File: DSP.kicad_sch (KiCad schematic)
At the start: 26 parts, among them J2 Conn_01x04, J3 Conn_01x04, J4 MEM2067-02-180-00-A_REVB, U4 STM32F401RBTx, U5 23K256, Y1 16MHz

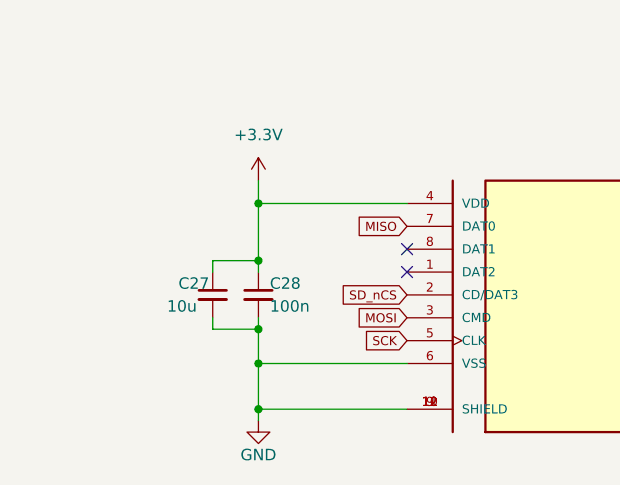
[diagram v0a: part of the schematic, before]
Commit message: added teardrops to increase yield&quality, also tuned usb data line skew
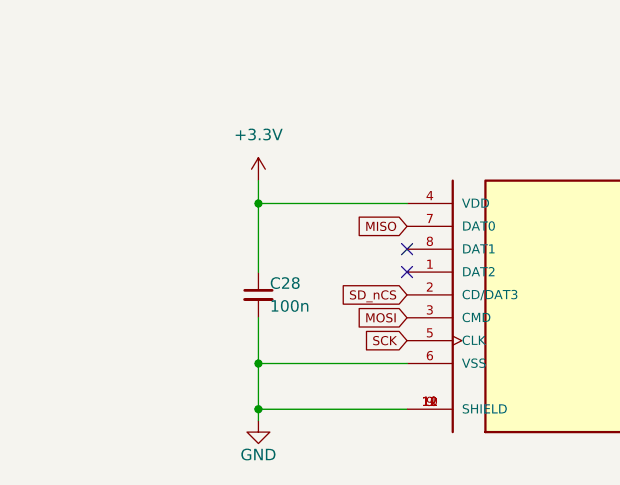
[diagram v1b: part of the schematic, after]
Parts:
- removed C27: 10u, Capacitor_SMD:C_0603_1608Metric_Pad1.08x0.95mm_HandSolder, symbol Device:C_Small
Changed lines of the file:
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@@
   (junction (at 60.96 36.83) (diameter 0) (color 0 0 0 0)
   )
-  (junction (at 53.34 161.29) (diameter 0) (color 0 0 0 0)
-  )
   (junction (at 30.48 40.64) (diameter 0) (color 0 0 0 0)
   )
@@
   )
   (junction (at 66.04 93.98) (diameter 0) (color 0 0 0 0)
-  )
-  (junction (at 53.34 168.91) (diameter 0) (color 0 0 0 0)
   )
   (junction (at 116.84 34.29) (diameter 0) (color 0 0 0 0)
@@
     (stroke (width 0) (type default))
   )
-  (wire (pts (xy 53.34 161.29) (xy 48.26 161.29))
-    (stroke (width 0) (type default))
-  )
   (wire (pts (xy 66.04 77.47) (xy 66.04 74.93))
     (stroke (width 0) (type default))
@@
     (stroke (width 0) (type default))
   )
-  (wire (pts (xy 53.34 168.91) (xy 53.34 172.72))
+  (wire (pts (xy 53.34 167.64) (xy 53.34 172.72))
     (stroke (width 0) (type default))
   )
@@
     (stroke (width 0) (type default))
   )
-  (wire (pts (xy 48.26 167.64) (xy 48.26 168.91))
-    (stroke (width 0) (type default))
-  )
   (wire (pts (xy 66.04 93.98) (xy 74.93 93.98))
     (stroke (width 0) (type default))
@@
     (stroke (width 0) (type default))
   )
-  (wire (pts (xy 48.26 161.29) (xy 48.26 162.56))
-    (stroke (width 0) (type default))
-  )
   (wire (pts (xy 92.71 53.34) (xy 92.71 52.07))
     (stroke (width 0) (type default))
@@
     (stroke (width 0) (type default))
   )
-  (wire (pts (xy 53.34 161.29) (xy 53.34 162.56))
-    (stroke (width 0) (type default))
-  )
   (wire (pts (xy 74.93 93.98) (xy 74.93 91.44))
     (stroke (width 0) (type default))
@@
     (stroke (width 0) (type default))
   )
-  (wire (pts (xy 53.34 168.91) (xy 48.26 168.91))
-    (stroke (width 0) (type default))
-  )
   (wire (pts (xy 214.63 97.79) (xy 214.63 99.06))
     (stroke (width 0) (type default))
@@
     (stroke (width 0) (type default))
   )
-  (wire (pts (xy 53.34 167.64) (xy 53.34 168.91))
-    (stroke (width 0) (type default))
-  )
   (wire (pts (xy 55.88 93.98) (xy 66.04 93.98))
     (stroke (width 0) (type default))
@@
     (stroke (width 0) (type default))
   )
-  (wire (pts (xy 53.34 154.94) (xy 53.34 161.29))
+  (wire (pts (xy 53.34 154.94) (xy 53.34 162.56))
     (stroke (width 0) (type default))
   )
@@
         )
       )
-    )
-  )
-  (symbol (lib_id "Device:C_Small") (at 48.26 165.1 0) (unit 1)
-    (in_bom yes) (on_board yes) (dnp no)
-    (property "Reference" "C27" (at 44.45 163.83 0)
-      (effects (font (size 1.27 1.27)) (justify left))
-    )
-    (property "Value" "10u" (at 43.18 166.37 0)
-      (effects (font (size 1.27 1.27)) (justify left))
-    )
-    (property "Footprint" "Capacitor_SMD:C_0603_1608Metric_Pad1.08x0.95mm_HandSolder" (at 48.26 165.1 0)
-      (effects (font (size 1.27 1.27)) hide)
-    )
-    (property "Datasheet" "~" (at 48.26 165.1 0)
-      (effects (font (size 1.27 1.27)) hide)
-    )
-    (pin "1")
-    (pin "2")
-    (instances
-      (project "Apollo - DSP"
-        (path "/e63e39d7-6ac0-4ffd-8aa3-1841a4541b55/65c41d2a-7921-40f6-8a66-43d43155f96a"
-          (reference "C27") (unit 1)
-        )
-      )

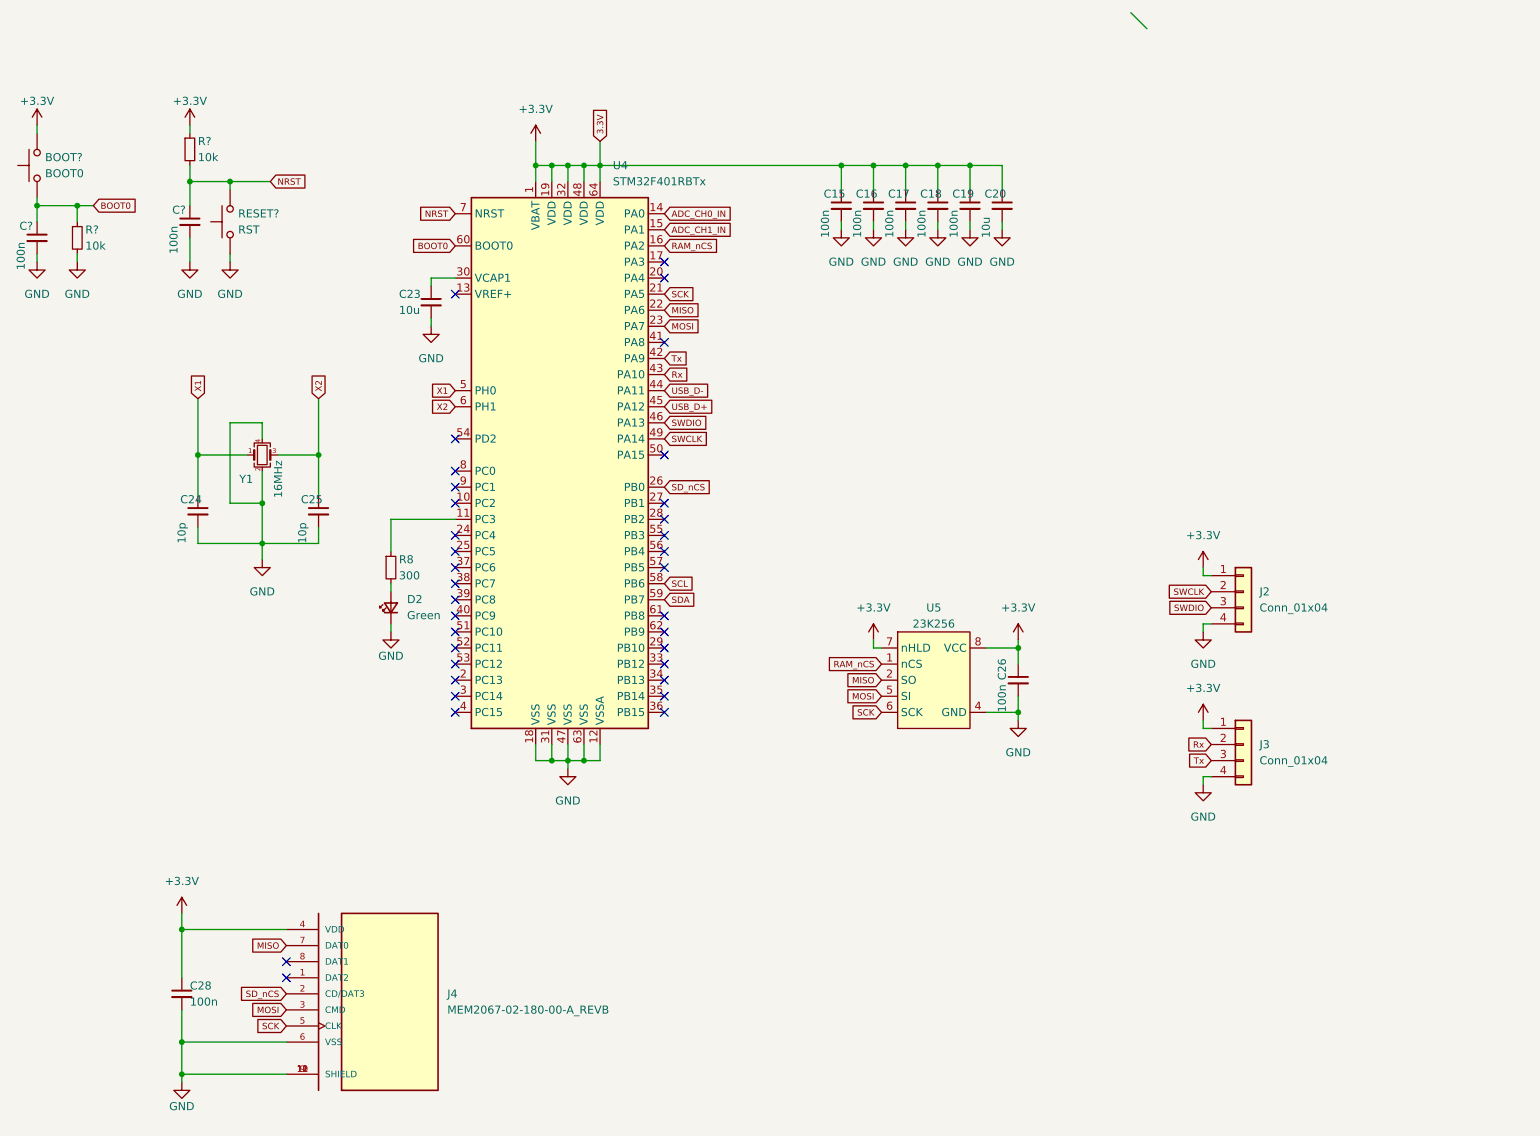
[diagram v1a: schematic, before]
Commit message: fixed bootloader setting to SWD, removed boot button.
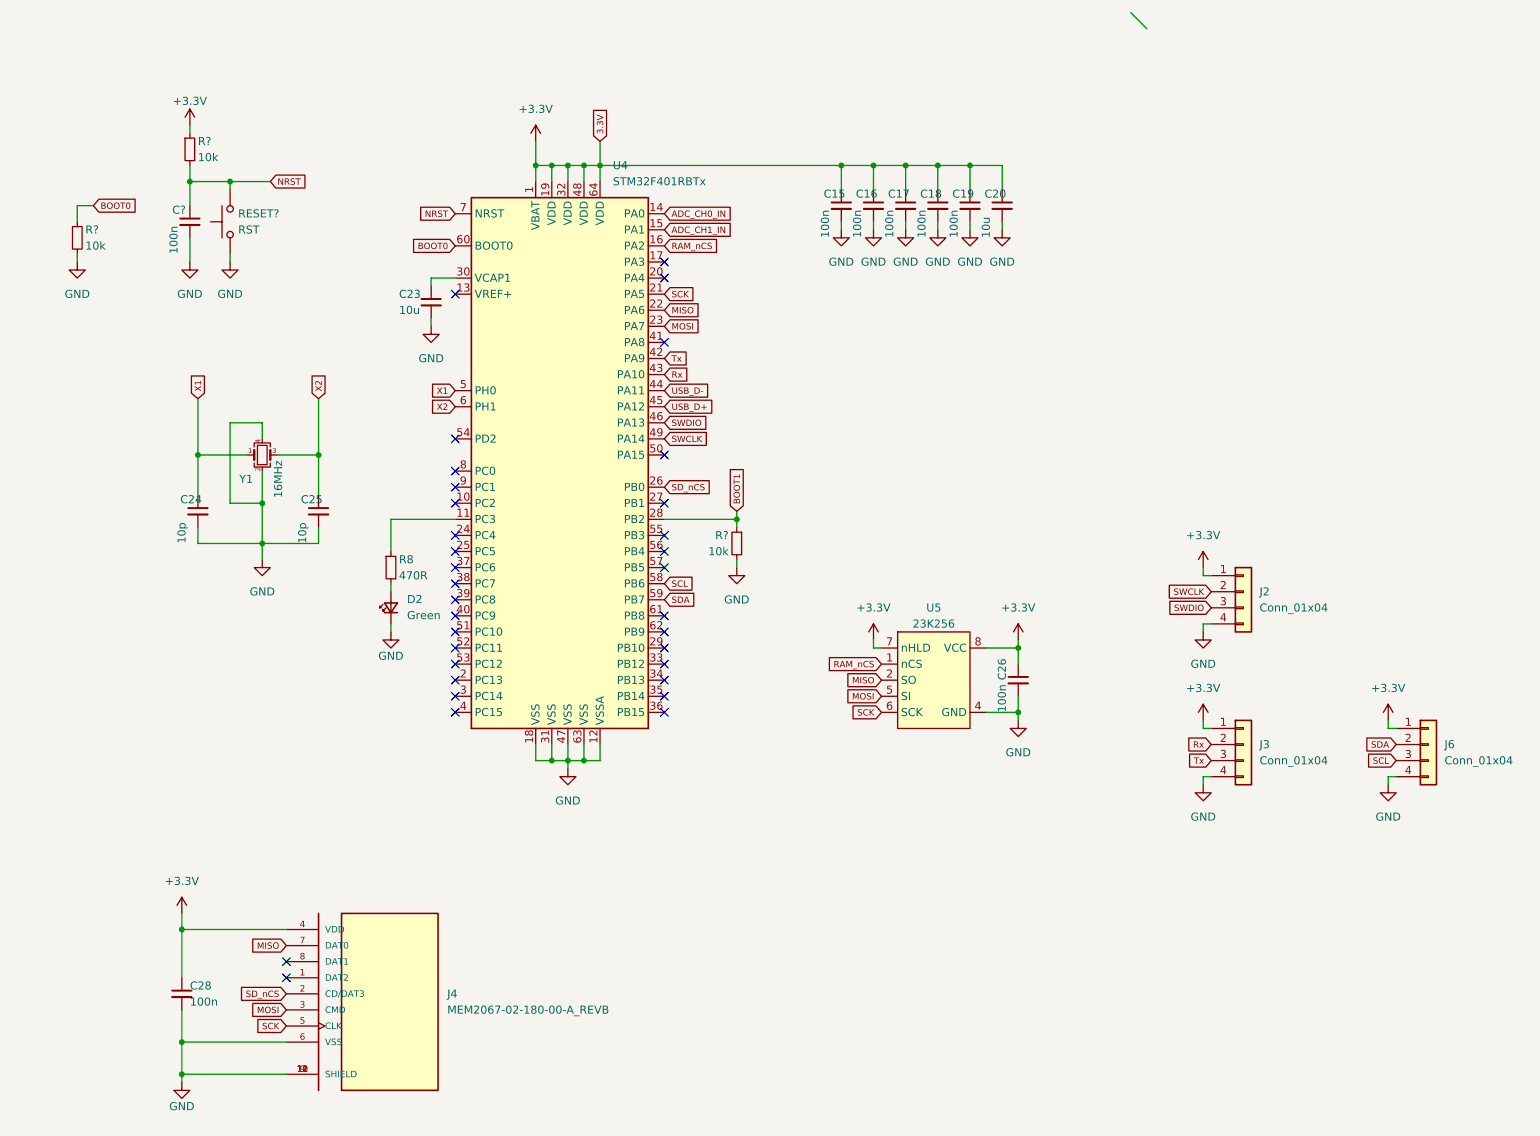
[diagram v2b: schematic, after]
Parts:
- removed BOOT?: BOOT0, Button_Switch_SMD:SW_SPST_TL3342, symbol Switch:SW_Push
- removed C?: 100n, Capacitor_SMD:C_0603_1608Metric_Pad1.08x0.95mm_HandSolder, symbol Device:C_Small
- added J6: Conn_01x04, Connector_PinHeader_2.54mm:PinHeader_1x04_P2.54mm_Vertical, symbol Connector_Generic:Conn_01x04
- added R?: 10k, Resistor_SMD:R_0603_1608Metric_Pad0.98x0.95mm_HandSolder, symbol Device:R_Small
- R8: value 300 -> 470R
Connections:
- net +3V3: now also J6.1 (Pin_1)
- net GND: now also J6.4 (Pin_4), R?.2
- net SCL: now also J6.3 (Pin_3)
- net SDA: now also J6.2 (Pin_2)
- net BOOT1: now reaches U4.28 (PB2)
- net BOOT1: now also R?.1
- no-connect marks 35 -> 34

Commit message: some changes
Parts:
- added R?: 10k, Resistor_SMD:R_0603_1608Metric_Pad0.98x0.95mm_HandSolder, symbol Device:R_Small
- R8: value 470R -> 1k
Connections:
- net +3V3: now also R?.1
- net BOOT1: now also R?.2
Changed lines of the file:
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@@
+    (stroke (width 0) (type default))
+  )
+  (wire (pts (xy 140.97 88.9) (xy 140.97 90.17))
     (stroke (width 0) (type default))
   )
@@
     (stroke (width 0) (type default))
   )
+  (wire (pts (xy 142.24 90.17) (xy 140.97 90.17))
+    (stroke (width 0) (type default))
+  )
   (wire (pts (xy 214.63 97.79) (xy 214.63 99.06))
     (stroke (width 0) (type default))
   )
-  (wire (pts (xy 140.97 90.17) (xy 140.97 88.9))
-    (stroke (width 0) (type default))
-  )
   (wire (pts (xy 177.8 43.18) (xy 177.8 44.45))
     (stroke (width 0) (type default))
@@
     (stroke (width 0) (type default))
   )
+  (wire (pts (xy 140.97 82.55) (xy 140.97 83.82))
+    (stroke (width 0) (type default))
+  )
   (wire (pts (xy 140.97 96.52) (xy 140.97 97.79))
     (stroke (width 0) (type default))
@@
     )
   )
-  (global_label "BOOT1" (shape input) (at 140.97 88.9 90) (fields_autoplaced)
-    (effects (font (size 1 1)) (justify left))
-    (property "Intersheetrefs" "${INTERSHEET_REFS}" (at 140.97 81.8026 90)
+  (global_label "BOOT1" (shape input) (at 142.24 90.17 0) (fields_autoplaced)
+    (effects (font (size 1 1)) (justify left))
+    (property "Intersheetrefs" "${INTERSHEET_REFS}" (at 149.3998 90.17 0)
       (effects (font (size 1 1)) (justify left) hide)
     )
@@
         (path "/e63e39d7-6ac0-4ffd-8aa3-1841a4541b55/65c41d2a-7921-40f6-8a66-43d43155f96a"
           (reference "C17") (unit 1)
+        )
+      )
+    )
+  )
+  (symbol (lib_id "Device:R_Small") (at 140.97 86.36 0) (mirror y) (unit 1)
+    (in_bom yes) (on_board yes) (dnp no)
+    (property "Reference" "R?" (at 146.05 83.82 0)
+      (effects (font (size 1.27 1.27)) (justify left))
+    )
+    (property "Value" "10k" (at 146.05 86.36 0)
+      (effects (font (size 1.27 1.27)) (justify left))
+    )
+    (property "Footprint" "Resistor_SMD:R_0603_1608Metric_Pad0.98x0.95mm_HandSolder" (at 140.97 86.36 0)
+      (effects (font (size 1.27 1.27)) hide)
+    )
+    (property "Datasheet" "~" (at 140.97 86.36 0)
+      (effects (font (size 1.27 1.27)) hide)
+    )
+    (pin "1")
+    (pin "2")
+    (instances
+      (project "STM32F103 devboard"
+        (path "/7cd8109f-5f99-46a5-9e32-14f7754144db"
+          (reference "R?") (unit 1)
+        )
+      )
+      (project "Apollo - DSP"
+        (path "/e63e39d7-6ac0-4ffd-8aa3-1841a4541b55/65c41d2a-7921-40f6-8a66-43d43155f96a"
+          (reference "R23") (unit 1)
         )
       )
@@
     )
   )
+  (symbol (lib_id "power:+3.3V") (at 140.97 82.55 0) (unit 1)
+    (in_bom yes) (on_board yes) (dnp no) (fields_autoplaced)
+    (property "Reference" "#PWR082" (at 140.97 86.36 0)
+      (effects (font (size 1.27 1.27)) hide)
+    )
+    (property "Value" "+3.3V" (at 140.97 77.47 0)
+      (effects (font (size 1.27 1.27)))
+    )
+    (property "Footprint" "" (at 140.97 82.55 0)
+      (effects (font (size 1.27 1.27)) hide)
+    )
+    (property "Datasheet" "" (at 140.97 82.55 0)
+      (effects (font (size 1.27 1.27)) hide)
+    )
+    (pin "1")
+    (instances
+      (project "Apollo - DSP"
+        (path "/e63e39d7-6ac0-4ffd-8aa3-1841a4541b55/65c41d2a-7921-40f6-8a66-43d43155f96a"
+          (reference "#PWR082") (unit 1)
+        )
+      )
+    )
+  )
   (symbol (lib_id "power:GND") (at 182.88 44.45 0) (unit 1)
     (in_bom yes) (on_board yes) (dnp no) (fields_autoplaced)
@@
       (effects (font (size 1.27 1.27)) (justify left))
     )
-    (property "Value" "470R" (at 87.63 99.06 0)
-      (effects (font (size 1.27 1.27)) (justify left))
-    )
+    (property "Value" "1k" (at 87.63 99.06 0)
+      (effects (font (size 1.27 1.27)) (justify left))
+    )
